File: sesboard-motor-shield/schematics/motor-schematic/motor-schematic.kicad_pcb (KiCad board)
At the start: 2 copper layers, 28 parts, among them J1 Barrel_Jack, J10 MOTOR_D_OUT, J11 STEPPER_TERMINAL, J2 EXTERNAL_MOTOR_POWER, J3 Conn_01x20_Female, J4 Conn_01x20_Female, J5 SERVO1, J6 SERVO2, J7 MOTOR_A_OUT, J8 MOTOR_B_OUT, J9 MOTOR_C_OUT, Q1 Q_NMOS_DGS, Q2 TIP3055, U1 LM317_SOT-223, U2 L293D, U3 L293D, U4 AMS1117-5.0, U5 L293D

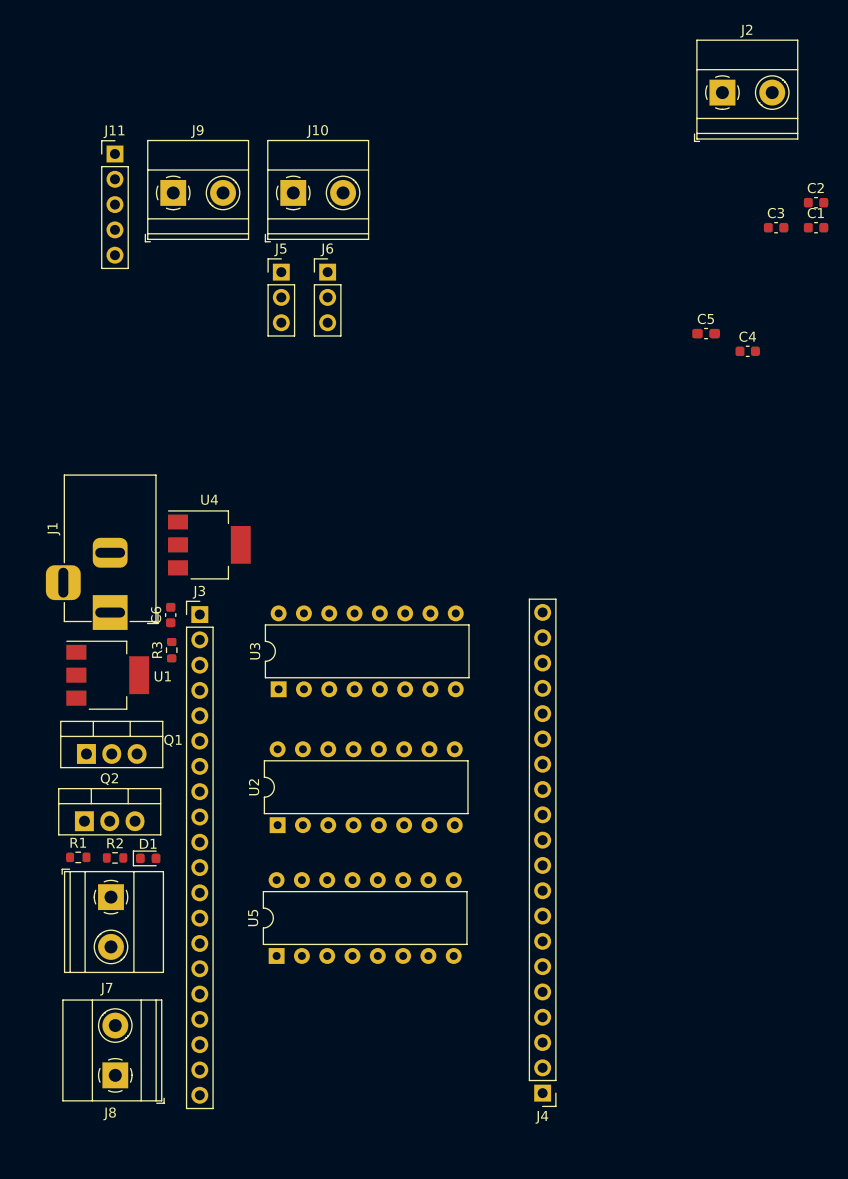
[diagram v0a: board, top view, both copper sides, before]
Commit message: added stepper connector
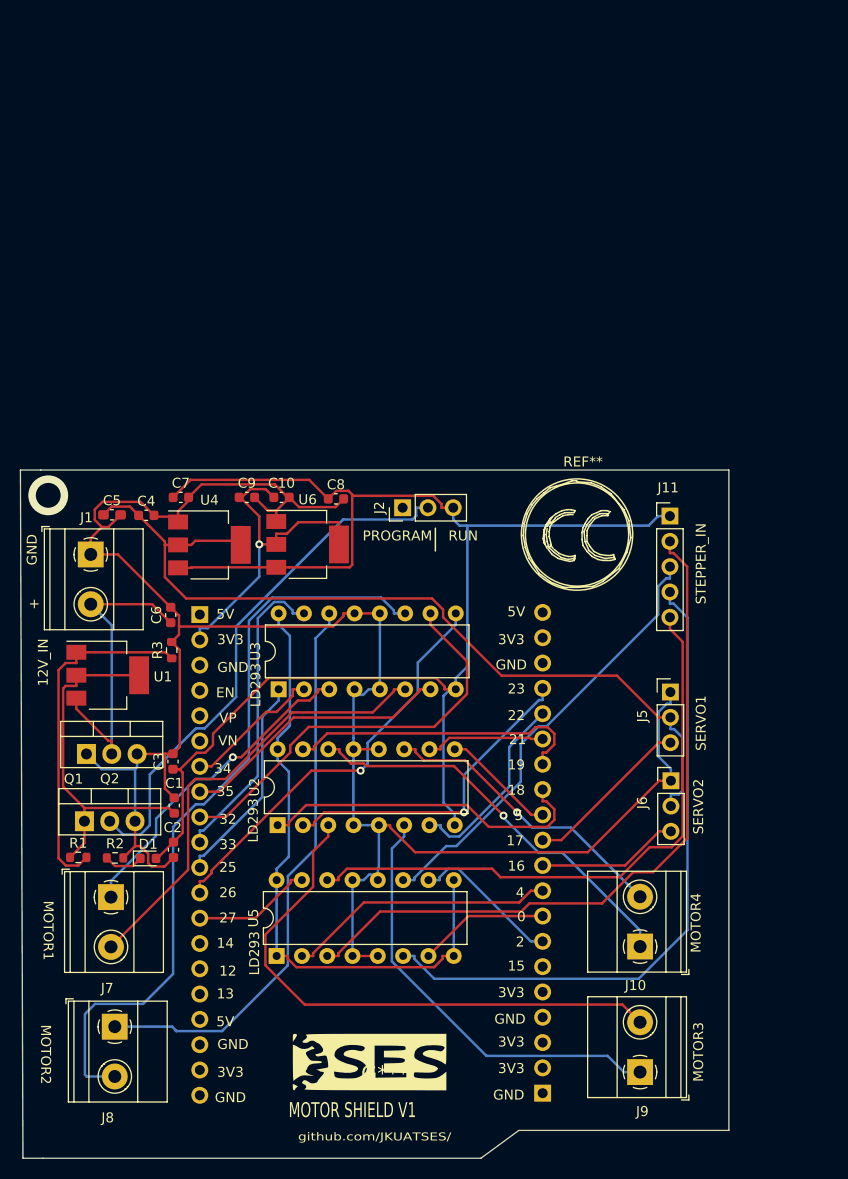
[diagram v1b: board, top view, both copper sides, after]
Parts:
- added C10: 10uF, Capacitor_SMD:C_0603_1608Metric, F.Cu at (86.4, 60.9)
- added C7: 10uF, Capacitor_SMD:C_0603_1608Metric, F.Cu at (76.3, 60.9)
- added C8: 10uF, Capacitor_SMD:C_0603_1608Metric, F.Cu at (91.9, 61.1)
- added C9: 10uF, Capacitor_SMD:C_0603_1608Metric, F.Cu at (82.9, 60.9)
- added G***: LOGO, custom-footprints:sesboard-logo, F.Cu at (96.8, 118.7)
- added REF**: Symbol_CreativeCommons_SilkScreenTop_Type2_Big, Symbol:Symbol_CreativeCommons_SilkScreenTop_Type2_Big, F.Cu at (116.1, 64.6)
- added U6: AMS1117-3.3, Package_TO_SOT_SMD:SOT-223-3_TabPin2, F.Cu at (89.0, 65.6)
- J1: value Barrel_Jack -> EXTERNAL_MOTOR_POWER; footprint Connector_BarrelJack:BarrelJack_Horizontal -> TerminalBlock_Phoenix:TerminalBlock_Phoenix_MKDS-1,5-2_1x02_P5.00mm_Horizontal
- J2: value EXTERNAL_MOTOR_POWER -> Conn_01x03_Female; footprint TerminalBlock_Phoenix:TerminalBlock_Phoenix_MKDS-1,5-2_1x02_P5.00mm_Horizontal -> Connector_PinHeader_2.54mm:PinHeader_1x03_P2.54mm_Vertical
- J3, J4: moved to B.Cu
- R2: value 510R -> 2K
- moved J9 99.9 mm to (122.4, 118.6), turned to 90 degrees
- moved C2 91.5 mm to (75.6, 96.3), turned to -90 degrees
- moved C1 86.7 mm to (75.6, 91.8), turned to 90 degrees
- moved J10 83.3 mm to (122.4, 106.0), turned to 90 degrees
- moved C3 80.9 mm to (75.5, 87.4), turned to 90 degrees
- moved J11 66.5 mm to (125.4, 62.8)
- moved C4 62.6 mm to (72.8, 62.7)
- moved C5 62.4 mm to (69.4, 62.7)
- moved J6 61.6 mm to (125.5, 89.4)
- moved J5 57.5 mm to (125.5, 80.5)
- moved J2 52.6 mm to (98.6, 62.0), turned to 90 degrees
- moved J1 6.15 mm to (67.3, 66.6)
- moved J8 4.89 mm to (69.7, 114.0), turned to -90 degrees
- turned J3 to 180 degrees
- turned J4 to 0 degrees
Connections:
- C6 pad 1: Net-(J1-Pad1) -> Net-(C6-Pad1)
- J1 pad 1: Net-(J1-Pad1) -> GND
- J1 pad 2: GND -> Net-(C6-Pad1)
- J2 pad 1: GND -> unconnected-(J2-Pad1)
- J2 pad 2: MOTOR_EXT+ -> Net-(Q2-Pad2)
- J3 pad 2: unconnected-(J3-Pad2) -> 3V3
- Q1 pad 2: Net-(J1-Pad1) -> Net-(C6-Pad1)
- Q2 pad 2: 12V -> Net-(Q2-Pad2)
- U1 pad 3: Net-(J1-Pad1) -> Net-(C6-Pad1)
- U2 pad 8: MOTOR_EXT+ -> 12V
- U3 pad 8: MOTOR_EXT+ -> 12V
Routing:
- net GND: track 0.00 -> 211.8 mm
- net 12V: track 0.00 -> 154.9 mm
- net SERVO_5V: track 0.00 -> 87.4 mm
- net MOTOR_B_OUT-: track 0.00 -> 76.2 mm
- net OUT1: track 0.00 -> 71.9 mm
- net OUT2: track 0.00 -> 66.6 mm
- net +5V: track 0.00 -> 63.0 mm
- net OUT4: track 0.00 -> 60.9 mm
- net MOTOR_B_OUT+: track 0.00 -> 57.4 mm
- net MOTOR_C_OUT+: track 0.00 -> 56.7 mm
- net Net-(Q2-Pad2): track 0.00 -> 53.7 mm
- net MOTOR_A_OUT-: track 0.00 -> 45.3 mm
- net OUT3: track 0.00 -> 44.5 mm
- net MOTOR_C_OUT-: track 0.00 -> 43.7 mm
- net IN3: track 0.00 -> 42.0 mm
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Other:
- board outline added: 71.1 x 69.1 mm
- board text added: "+"
- board text added: "0"
- board text added: "12"
- board text added: "12V_IN"
- board text added: "13"
- board text added: "14"
- board text added: "15"
- board text added: "16"
- board text added: "17"
- board text added: "18"
- board text added: "19"
- board text added: "2"
- board text added: "21"
- board text added: "22"
- board text added: "23"
- board text added: "25"
- board text added: "26"
- board text added: "27"
- board text added: "32"
- board text added: "33"
- board text added: "34"
- board text added: "35"
- board text added: "3V3"
- board text added: "4"
- board text added: "5"
- board text added: "5V"
- board text added: "EN"
- board text added: "GND"
- board text added: "LD293"
- board text added: "MOTOR SHIELD V1"
- board text added: "MOTOR1"
- board text added: "MOTOR2"
- board text added: "MOTOR3"
- board text added: "MOTOR4"
- board text added: "PROGRAM"
- board text added: "RUN"
- board text added: "SERVO1"
- board text added: "SERVO2"
- board text added: "STEPPER_IN"
- board text added: "VN"
- board text added: "VP"
- board text added: "github.com/JKUATSES/"

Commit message: added view image
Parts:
- removed REF**: Symbol_CreativeCommons_SilkScreenTop_Type2_Big, Symbol:Symbol_CreativeCommons_SilkScreenTop_Type2_Big
- J1, J10, J7, J8, J9: moved to B.Cu
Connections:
- C7 pad 1: 12V -> SERVO_5V
- C8 pad 1: 12V -> SERVO_5V
- U6 pad 3: 12V -> SERVO_5V
